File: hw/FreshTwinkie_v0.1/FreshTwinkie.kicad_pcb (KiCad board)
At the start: 2 copper layers, 40.2 x 35.5 mm, 54 parts, among them J1 USB_C_Receptacle, J2 USB_B_Micro, P1 USB_C_Plug, Q1 BSD84, Q2 BSD84, Q3 BSD84, Q4 BSD84, SW1 SW_Push, U1 AD860, U2 STM32F072CBUx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

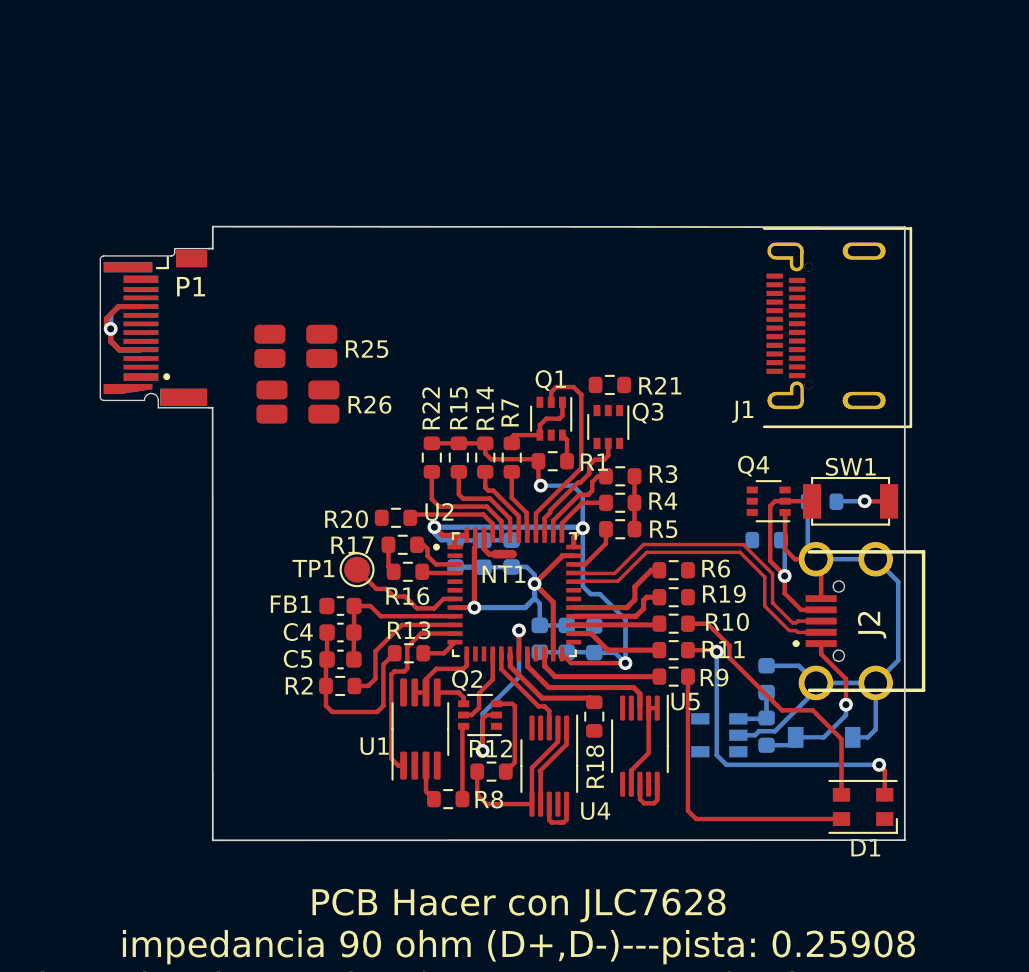
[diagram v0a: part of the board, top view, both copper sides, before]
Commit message: changeUSB-CReceptacle
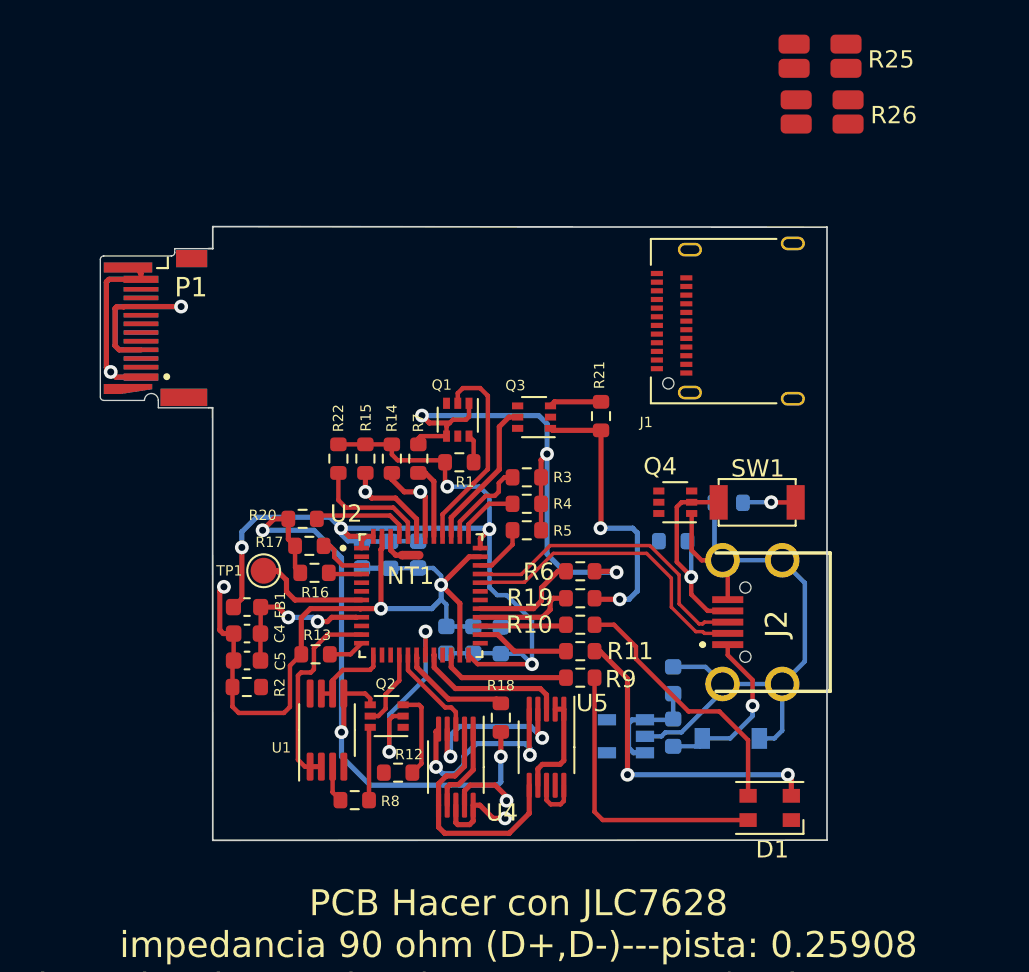
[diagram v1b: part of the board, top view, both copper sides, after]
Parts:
- J1: footprint Footprint:XUNPU_24PIN_USBC_RECEPT -> Connector_USB:USB_C_Receptacle_Amphenol_12401610E4-2A
- Q1, Q2, Q3, Q4: value BSD84 -> BSD840NH6327XTSA1
- U1: value AD860 -> AD8606ARMZ-REEL
- moved R25 34.6 mm to (171.2, 80.2)
- moved R26 34.6 mm to (171.4, 83.4)
- moved J1 6.20 mm to (166.8, 95.5)
- moved C1 5.40 mm to (148.0, 109.0)
- moved C2 5.40 mm to (146.4, 109.0)
- moved C3 5.40 mm to (144.8, 109.0)
- moved C4 5.40 mm to (138.1, 113.6)
- moved C5 5.40 mm to (138.1, 115.1)
- moved C6 5.40 mm to (149.6, 113.9)
- moved C7 5.40 mm to (151.2, 113.9)
- moved C8 5.40 mm to (162.8, 116.3)
- moved C9 5.40 mm to (152.8, 114.0)
- moved FB1 5.40 mm to (138.1, 112.0)
- moved FB2 5.40 mm to (162.8, 119.3)
- moved J2 5.40 mm to (168.1, 112.9)
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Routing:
- net /CC2: track 3.69 -> 56.0 mm, vias 0 -> 5
- net GND: track 87.7 -> 117.8 mm, vias 2 -> 4
- net /CC1: track 10.1 -> 34.1 mm, vias 0 -> 3
- net +3V3: track 58.7 -> 73.9 mm, vias 4 -> 5
- net /SCL: track 4.63 -> 17.0 mm, vias 0 -> 3
- net /SDA: track 5.81 -> 16.1 mm, vias 0 -> 3
- net /CC1_EN: track 8.20 -> 0.00 mm
- net Net-(P1-PadA4): track 11.1 -> 15.2 mm
- net /USBC_CC2_-: track 0.00 -> 3.91 mm, vias 0 -> 1
- net Net-(C8-Pad1): track 3.12 -> 6.63 mm
- net Net-(Q3-Pad3): track 0.00 -> 3.02 mm
- net /USBC_CC2_+: track 2.94 -> 5.22 mm, vias 0 -> 1
- net /CC2_TX_EN: track 7.23 -> 8.78 mm
- net /CC1_BUF: track 11.1 -> 11.8 mm
- net Net-(C4-Pad1): track 9.17 -> 9.08 mm, vias 0 -> 2
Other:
- board size 40.2 x 35.5 mm -> 35.8 x 35.5 mm

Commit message: RearrengePCB
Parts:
- D2, FB2, U3: moved to F.Cu
- Q1, Q2, Q3: value BSD840NH6327XTSA1 -> BSD84
- Q4: value BSD840NH6327XTSA1 -> BSD84; moved to B.Cu
- R12, R13, R16, R17, R18, R2, R20, R22, R25, R26, R8: moved to B.Cu
- moved U5 61.0 mm to (214.9, 106.8), turned to 0 degrees
- moved R24 60.8 mm to (226.8, 106.9), turned to 270 degrees
- moved U4 59.3 mm to (207.7, 106.8), turned to 180 degrees
- moved R8 59.1 mm to (202.9, 115.7), turned to 180 degrees
- moved R23 59.0 mm to (221.7, 106.8), turned to 180 degrees
- moved NT1 57.6 mm to (204.5, 100.6)
- moved J2 56.8 mm to (224.9, 113.2)
- moved SW1 55.4 mm to (225.2, 107.5)
- moved Q4 54.8 mm to (217.7, 106.3)
- moved C8 54.8 mm to (217.5, 114.4)
- moved FB2 52.9 mm to (215.4, 115.0), turned to 90 degrees
- moved U3 52.6 mm to (212.5, 116.8)
- moved D1 52.5 mm to (220.8, 120.8)
- moved C3 52.2 mm to (196.9, 110.7), turned to 180 degrees
- moved R2 52.1 mm to (190.2, 117.1)
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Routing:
- net GND: track 117.8 -> 61.8 mm, vias 4 -> 1
- net /CC2: track 56.0 -> 29.2 mm, vias 5 -> 4
- net /CC1: track 34.1 -> 14.7 mm, vias 3 -> 2
- net +3V3: track 73.9 -> 60.3 mm, vias 5 -> 4
- net /SCL: track 17.0 -> 4.07 mm, vias 3 -> 0
- net Net-(Q2-Pad6): track 4.24 -> 15.9 mm, vias 0 -> 1
- net /SDA: track 16.1 -> 5.06 mm, vias 3 -> 0
- net /VBUS_ALERT_L: track 8.71 -> 0.00 mm
- net /USB_B_D-: track 17.9 -> 25.9 mm
- net /USB_B_D+: track 17.9 -> 25.9 mm
- net /CC1_BUF: track 11.8 -> 3.97 mm
- net /CC1_TX_DATA: track 11.8 -> 5.12 mm
- net /CC2_ALERT_L: track 5.63 -> 0.00 mm
- net /USBC_CC2_+: track 5.22 -> 0.00 mm, vias 1 -> 0
- net /BOOT: track 6.94 -> 2.62 mm, vias 0 -> 1
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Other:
- outline, holes or cut-outs redrawn

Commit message: routeResistorShout
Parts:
- R10, R11, R19, R6, R9: moved to B.Cu
- R25, R26: moved to F.Cu
- moved U5 72.7 mm to (142.3, 104.7), turned to 180 degrees
- moved U4 65.4 mm to (142.3, 108.3)
- moved D1 63.5 mm to (157.3, 117.9), turned to 0 degrees
- moved FB2 60.9 mm to (155.2, 123.4)
- moved U3 60.6 mm to (152.1, 122.2)
- moved SW1 60.0 mm to (165.2, 106.9)
- moved J2 59.6 mm to (165.4, 113.6)
- moved D2 59.5 mm to (158.4, 122.2), turned to 0 degrees
- moved R24 59.5 mm to (167.3, 105.4)
- moved NT1 58.3 mm to (147.9, 114.2), turned to 90 degrees
- moved Q4 56.9 mm to (160.8, 105.6)
- moved R23 56.9 mm to (164.8, 106.1)
- moved C8 55.9 mm to (161.9, 120.3)
- moved R8 53.0 mm to (150.5, 123.3)
- moved R10 46.3 mm to (156.6, 116.8)
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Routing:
- net GND: track 61.8 -> 154.5 mm, vias 1 -> 9
- net /CC1: track 14.7 -> 44.4 mm, vias 2 -> 5
- net /CC1_EN: track 2.41 -> 31.4 mm, vias 1 -> 2
- net /USBC_VBUS_-: track 0.00 -> 21.8 mm, vias 0 -> 2
- net /USBC_CC2_+: track 0.00 -> 18.5 mm
- net /CC2: track 29.2 -> 46.3 mm, vias 4 -> 3
- net /USBC_CC2_-: track 0.00 -> 15.5 mm
- net /USB_B_D-: track 25.9 -> 10.9 mm
- net /USB_B_D+: track 25.9 -> 10.9 mm
- net Net-(D1-Pad2): track 21.0 -> 7.04 mm, vias 2 -> 1
- net /USBC_VBUS_+: track 0.00 -> 12.7 mm
- net Net-(D1-Pad3): track 16.8 -> 5.27 mm, vias 0 -> 1
- net /SDA: track 5.06 -> 15.9 mm
- net Net-(D1-Pad4): track 15.9 -> 6.66 mm, vias 0 -> 1
- net Net-(Q2-Pad6): track 15.9 -> 6.72 mm
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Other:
- board size 35.8 x 35.5 mm -> 32.8 x 35.5 mm

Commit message: routeGND
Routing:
- net +3V3: track 65.7 -> 86.2 mm
- net /CC1: track 44.4 -> 58.8 mm, vias 5 -> 6
- net Net-(D2-Pad1): track 1.76 -> 13.6 mm
- net GND: track 154.5 -> 164.6 mm
- net /CC2: track 46.3 -> 46.8 mm, vias 3 -> 4
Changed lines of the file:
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@@
     (thickness 0.8)
     (drawings 9)
-    (tracks 602)
+    (tracks 645)
     (zones 0)
     (modules 54)
@@
     (effects (font (size 1.5 1.5) (thickness 0.375)))
   )
-  (via (at 148.11 122.49) (size 0.5) (drill 0.2) (layers F.Cu B.Cu) (net 2))
   (via (at 151.98 122.25) (size 0.5) (drill 0.2) (layers F.Cu B.Cu) (net 1))
   (via (at 147.18 119.97) (size 0.5) (drill 0.2) (layers F.Cu B.Cu) (net 35))
@@
   (segment (start 150.81 122.22) (end 151.95 122.22) (width 0.3) (layer B.Cu) (net 1))
   (segment (start 153.23 122.25) (end 151.98 122.25) (width 0.3) (layer F.Cu) (net 1))
+  (segment (start 160.05 122.22) (end 160.05 121.11) (width 0.3) (layer F.Cu) (net 1))
+  (segment (start 160.05 121.11) (end 161.28 119.88) (width 0.3) (layer F.Cu) (net 1))
+  (segment (start 161.28 119.88) (end 162.09 119.88) (width 0.3) (layer F.Cu) (net 1))
+  (segment (start 162.875 119.095) (end 162.875 117.155) (width 0.3) (layer F.Cu) (net 1))
+  (segment (start 162.09 119.88) (end 162.875 119.095) (width 0.3) (layer F.Cu) (net 1))
+  (segment (start 165.95 102.141998) (end 164.981999 103.109999) (width 0.3) (layer B.Cu) (net 1))
+  (segment (start 165.95 100.16) (end 165.95 102.141998) (width 0.3) (layer B.Cu) (net 1))
   (segment (start 146.43 105.615) (end 147.96 105.615) (width 0.5) (layer F.Cu) (net 2))
   (segment (start 147.96 105.615) (end 147.96 103.83) (width 0.5) (layer F.Cu) (net 2))
@@
   (segment (start 150.08 123.2) (end 151.03 123.2) (width 0.3) (layer F.Cu) (net 2))
   (segment (start 150 123.12) (end 150.08 123.2) (width 0.3) (layer F.Cu) (net 2))
-  (segment (start 148.08 122.52) (end 148.11 122.49) (width 0.3) (layer B.Cu) (net 2))
+  (segment (start 145.99499 121.69499) (end 143.62501 121.69499) (width 0.3) (layer B.Cu) (net 2))
+  (segment (start 146.82 122.52) (end 145.99499 121.69499) (width 0.3) (layer B.Cu) (net 2))
+  (via (at 142.98 123.36) (size 0.8) (drill 0.4) (layers F.Cu B.Cu) (net 2))
+  (segment (start 142.98 122.34) (end 142.98 123.36) (width 0.3) (layer B.Cu) (net 2))
+  (segment (start 143.62501 121.69499) (end 142.98 122.34) (width 0.3) (layer B.Cu) (net 2))
+  (segment (start 138.4425 115.71) (end 137.7 115.71) (width 0.3) (layer F.Cu) (net 2))
+  (segment (start 137.7 115.71) (end 137.34 116.07) (width 0.3) (layer F.Cu) (net 2))
+  (segment (start 137.34 116.07) (end 137.34 123.9) (width 0.3) (layer F.Cu) (net 2))
+  (segment (start 142.259999 124.080001) (end 142.98 123.36) (width 0.3) (layer F.Cu) (net 2))
+  (segment (start 137.520001 124.080001) (end 142.259999 124.080001) (width 0.3) (layer F.Cu) (net 2))
+  (segment (start 137.34 123.9) (end 137.520001 124.080001) (width 0.3) (layer F.Cu) (net 2))
   (segment (start 140.3375 115.39) (end 140.0175 115.71) (width 0.3) (layer F.Cu) (net 3))
   (segment (start 145.78 115.39) (end 140.3375 115.39) (width 0.3) (layer F.Cu) (net 3))
@@
   (segment (start 156.3375 122.6325) (end 156.75 122.22) (width 0.3) (layer F.Cu) (net 8))
   (segment (start 155.16 122.6325) (end 156.3375 122.6325) (width 0.3) (layer F.Cu) (net 8))
+  (segment (start 163.175 114.88) (end 163.175 115.225) (width 0.3) (layer F.Cu) (net 8))
+  (segment (start 163.175 115.225) (end 162.72 115.68) (width 0.3) (layer F.Cu) (net 8))
+  (segment (start 162.72 115.68) (end 161.61 115.68) (width 0.3) (layer F.Cu) (net 8))
+  (segment (start 161.310001 115.979999) (end 161.310001 118.319999) (width 0.3) (layer F.Cu) (net 8))
+  (segment (start 161.61 115.68) (end 161.310001 115.979999) (width 0.3) (layer F.Cu) (net 8))
+  (segment (start 161.310001 118.319999) (end 159.51 120.12) (width 0.3) (layer F.Cu) (net 8))
+  (segment (start 159.51 120.12) (end 157.53 120.12) (width 0.3) (layer F.Cu) (net 8))
+  (segment (start 156.75 120.9) (end 156.75 122.22) (width 0.3) (layer F.Cu) (net 8))
+  (segment (start 157.53 120.12) (end 156.75 120.9) (width 0.3) (layer F.Cu) (net 8))
   (segment (start 153.292501 113.39) (end 153.317501 113.365) (width 0.2) (layer F.Cu) (net 24))
   (segment (start 152.64 113.39) (end 153.292501 113.39) (width 0.2) (layer F.Cu) (net 24))
@@
   (segment (start 141.440011 124.700011) (end 151.059989 124.700011) (width 0.3) (layer B.Cu) (net 32))
   (segment (start 142.2 119.01) (end 140.97 119.01) (width 0.3) (layer B.Cu) (net 32))
+  (segment (start 158.73 115.35) (end 158.07 115.35) (width 0.3) (layer F.Cu) (net 32))
+  (segment (start 158.07 115.35) (end 157.35 116.07) (width 0.3) (layer F.Cu) (net 32))
+  (segment (start 157.35 116.07) (end 157.35 119.4) (width 0.3) (layer F.Cu) (net 32))
+  (segment (start 157.35 119.4) (end 157.35 119.59288) (width 0.3) (layer F.Cu) (net 32))
+  (segment (start 155.688001 121.410001) (end 154.770001 121.410001) (width 0.3) (layer F.Cu) (net 32))
+  (segment (start 156.000001 121.098001) (end 155.688001 121.410001) (width 0.3) (layer F.Cu) (net 32))
+  (segment (start 156.000001 120.942879) (end 156.000001 121.098001) (width 0.3) (layer F.Cu) (net 32))
+  (segment (start 157.35 119.59288) (end 156.000001 120.942879) (width 0.3) (layer F.Cu) (net 32))
+  (via (at 154.5 120.81) (size 0.5) (drill 0.2) (layers F.Cu B.Cu) (net 32))
+  (segment (start 154.5 121.14) (end 154.5 120.81) (width 0.3) (layer F.Cu) (net 32))
+  (segment (start 154.770001 121.410001) (end 154.5 121.14) (width 0.3) (layer F.Cu) (net 32))
+  (segment (start 151.365 123.3) (end 153.57 123.3) (width 0.3) (layer B.Cu) (net 32))
+  (segment (start 154.5 122.37) (end 154.5 120.81) (width 0.3) (layer B.Cu) (net 32))
+  (segment (start 153.57 123.3) (end 154.5 122.37) (width 0.3) (layer B.Cu) (net 32))
   (segment (start 150.795 106.35) (end 150.46 106.685) (width 0.3) (layer F.Cu) (net 33))
   (segment (start 150.46 106.685) (end 150.46 110.71) (width 0.3) (layer F.Cu) (net 33))
@@
   (segment (start 142.260001 124.200001) (end 141.54 123.48) (width 0.3) (layer B.Cu) (net 36))
   (segment (start 147.779999 124.200001) (end 142.260001 124.200001) (width 0.3) (layer B.Cu) (net 36))
-  (segment (start 148.71 119.94) (end 148.71 123.18) (width 0.3) (layer F.Cu) (net 36))
-  (segment (start 148.71 123.18) (end 148.26 123.63) (width 0.3) (layer F.Cu) (net 36))
-  (segment (start 148.26 123.63) (end 147.3 123.63) (width 0.3) (layer F.Cu) (net 36))
-  (segment (start 147.05 123.38) (end 147.05 122.48) (width 0.3) (layer F.Cu) (net 36))
-  (segment (start 147.3 123.63) (end 147.05 123.38) (width 0.3) (layer F.Cu) (net 36))
+  (segment (start 147.05 122.48) (end 147.88 122.48) (width 0.3) (layer F.Cu) (net 36))
+  (segment (start 148.71 121.65) (end 148.71 119.94) (width 0.3) (layer F.Cu) (net 36))
+  (segment (start 147.88 122.48) (end 148.71 121.65) (width 0.3) (layer F.Cu) (net 36))
+  (segment (start 147.779999 124.200001) (end 148.319999 124.200001) (width 0.3) (layer B.Cu) (net 36))
+  (via (at 148.59 122.82) (size 0.5) (drill 0.2) (layers F.Cu B.Cu) (net 36))
+  (segment (start 148.59 123.93) (end 148.59 122.82) (width 0.3) (layer B.Cu) (net 36))
+  (segment (start 148.319999 124.200001) (end 148.59 123.93) (width 0.3) (layer B.Cu) (net 36))
+  (segment (start 148.22 122.82) (end 147.88 122.48) (width 0.3) (layer F.Cu) (net 36))
+  (segment (start 148.59 122.82) (end 148.22 122.82) (width 0.3) (layer F.Cu) (net 36))
   (segment (start 144.525 121.83) (end 144.21 122.145) (width 0.3) (layer F.Cu) (net 37))
   (segment (start 145.15 121.83) (end 144.525 121.83) (width 0.3) (layer F.Cu) (net 37))

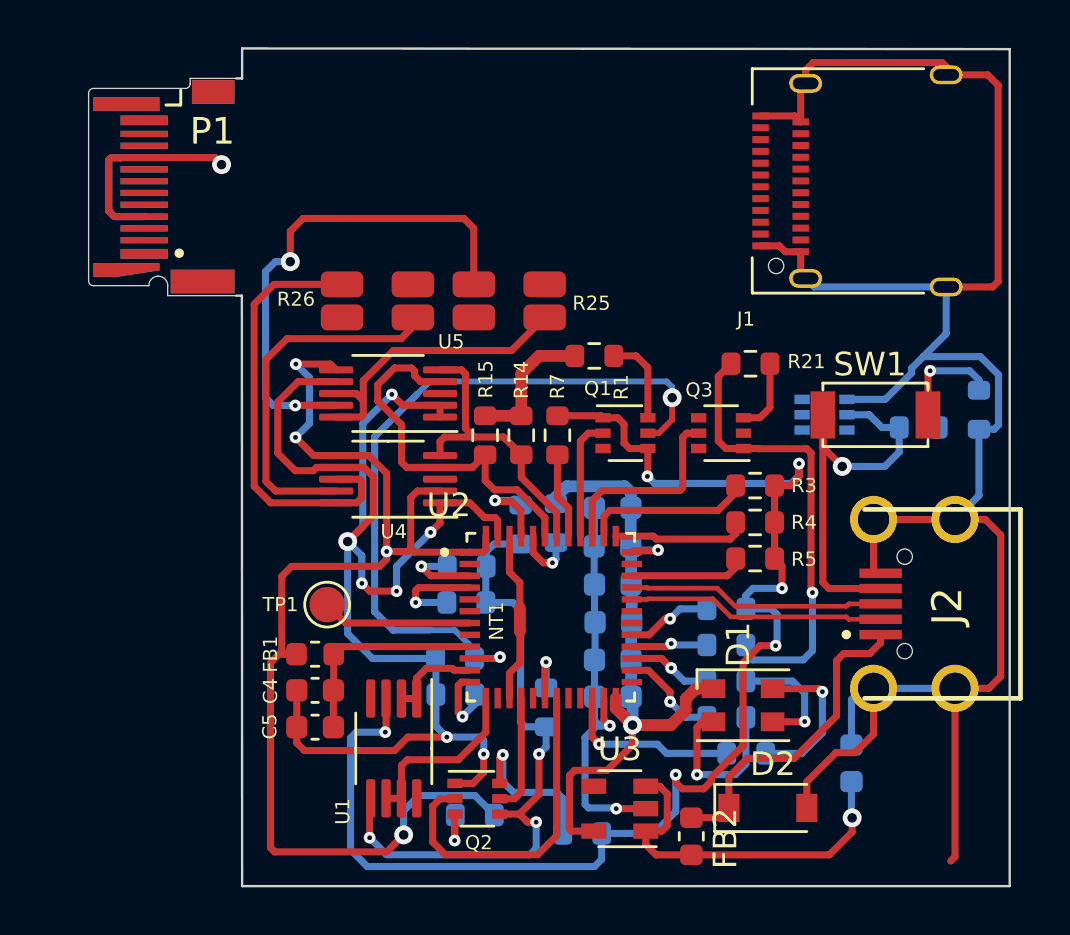
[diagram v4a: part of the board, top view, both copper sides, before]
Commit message: routeUSBCR&P
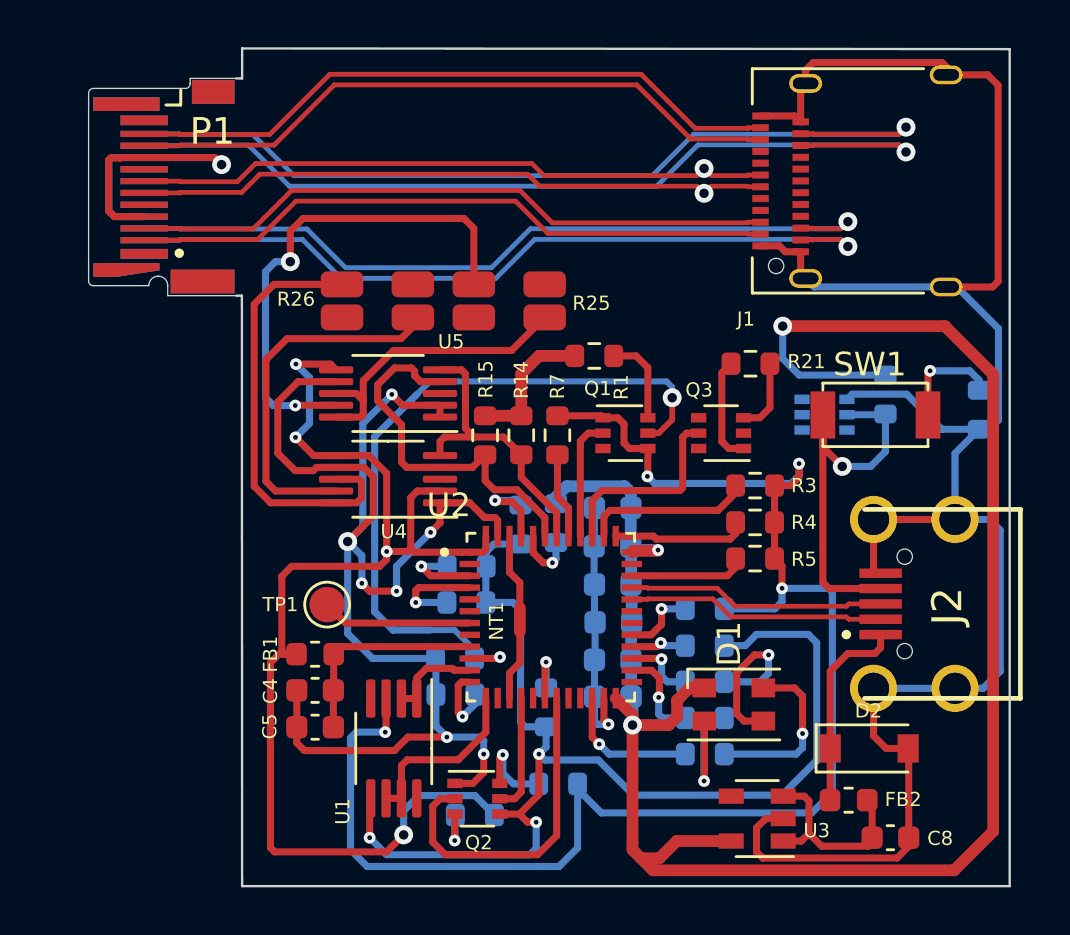
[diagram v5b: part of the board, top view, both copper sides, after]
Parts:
- C8: moved to F.Cu
- moved FB2 6.83 mm to (161.8, 121.9), turned to 180 degrees
- moved U3 5.84 mm to (157.9, 122.7)
- moved D2 4.98 mm to (162.7, 119.7)
- moved C8 3.56 mm to (163.6, 123.5), turned to 0 degrees
- moved R8 2.33 mm to (149.5, 121.2)
- moved R23 1.98 mm to (163.4, 104.7), turned to 270 degrees
- moved R9 1.76 mm to (155.7, 119.9)
- moved R10 0.92 mm to (155.7, 116.9)
- moved R11 0.92 mm to (155.7, 118.4)
- moved R19 0.92 mm to (155.7, 115.3)
- moved R6 0.92 mm to (155.7, 113.8)
- moved D1 0.39 mm to (157.0, 117.8)
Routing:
- net +3V3: track 86.2 -> 139.4 mm, vias 6 -> 7
- net /TX2-: track 0.00 -> 38.4 mm, vias 0 -> 1
- net /TX2+: track 0.00 -> 38.4 mm, vias 0 -> 1
- net /RX1+: track 0.00 -> 33.4 mm, vias 0 -> 1
- net /RX1-: track 0.00 -> 33.4 mm, vias 0 -> 1
- net /RX2-: track 0.00 -> 28.1 mm
- net /RX2+: track 0.00 -> 28.1 mm
- net /TX1+: track 0.00 -> 27.4 mm
- net /TX1-: track 0.00 -> 27.4 mm
- net /USBC_D+: track 0.00 -> 26.9 mm, vias 0 -> 1
- net /USBC_D-: track 0.00 -> 26.9 mm, vias 0 -> 1
- net /CC2: track 46.8 -> 54.2 mm, vias 4 -> 3
- net /CC1: track 58.8 -> 65.8 mm, vias 6 -> 4
- net Net-(C8-Pad1): track 15.4 -> 8.62 mm, vias 1 -> 0
- net GND: track 164.6 -> 158.0 mm, vias 9 -> 8
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
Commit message: RearrengeR6,9,10,11
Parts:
- moved R25 1.46 mm to (148.9, 100.5)
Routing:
- net Net-(J1-PadA4): track 0.00 -> 22.4 mm, vias 0 -> 2
- net GND: track 158.0 -> 177.9 mm, vias 8 -> 9
- net /USBC_D-: track 26.9 -> 43.6 mm, vias 1 -> 2
- net /USBC_D+: track 26.9 -> 40.3 mm, vias 1 -> 2
- net /USBC_CC2: track 0.00 -> 6.78 mm, vias 0 -> 1
- net /USB_C_SBU2: track 0.00 -> 6.04 mm, vias 0 -> 1
- net /USBC_VBUS_+: track 12.7 -> 14.7 mm
